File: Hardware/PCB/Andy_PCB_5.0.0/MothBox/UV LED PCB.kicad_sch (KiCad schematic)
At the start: 24 parts, among them J7 DC Power Jack, Q10 BC817, Q11 BC817, Q8 BC817, Q9 BC817, U10 IRF9335TRPBF, U11 IRF9335TRPBF, U8 IRF9335TRPBF, U9 IRF9335TRPBF

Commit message: made better camera
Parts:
- renumbered D29 to D30, D30 to D32, D36 to D33, J7 to J5, Q9 to Q10, Q10 to Q11, Q11 to Q9, R80 to R76, R82 to R78, R76 to R79, R81 to R80, R78 to R81, R79 to R82, U8 to U10, U9 to U12, U10 to U13

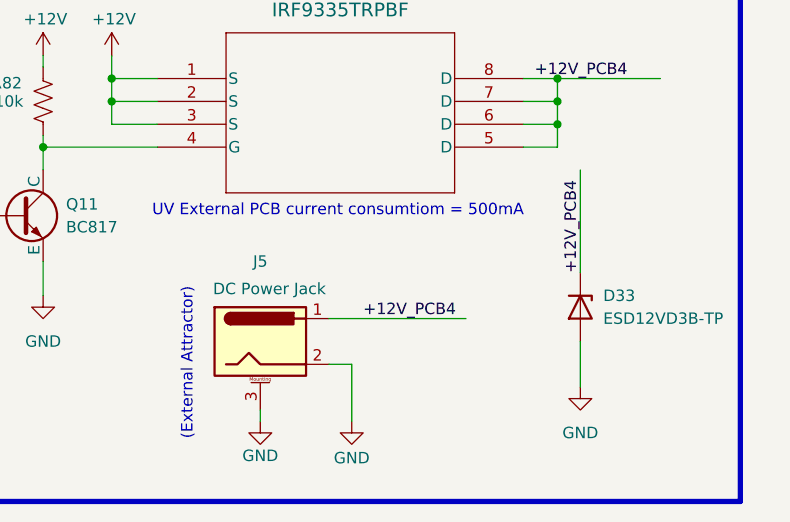
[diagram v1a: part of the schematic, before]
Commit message: added female inverted header
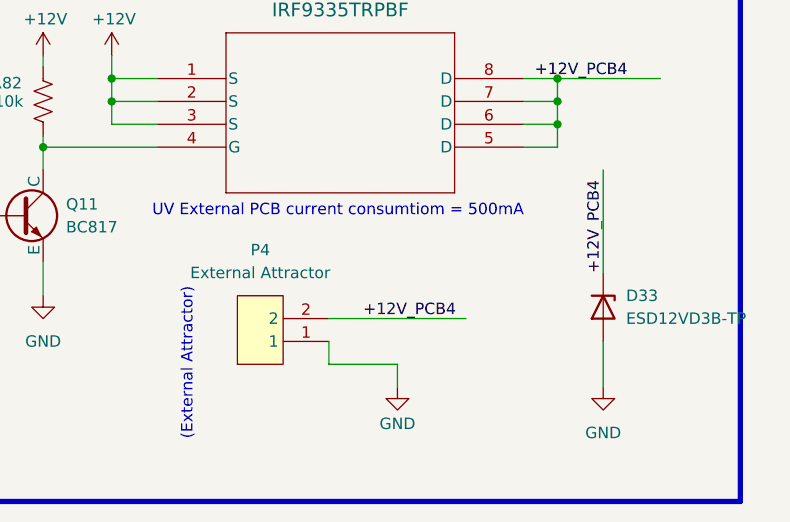
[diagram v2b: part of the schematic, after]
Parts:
- removed J5: DC Power Jack, Connector_BarrelJack:BarrelJack_GCT_DCJ200-10-A_Horizontal, symbol Connector:Barrel_Jack_MountingPin
- added P4: External Attractor, easyeda2kicad:CONN-TH_2P-P5.00_WJ500V-5.08-2P, symbol easyeda2kicad:WJ500V-5.08-2P-14-00A
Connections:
- net +12V_PCB4: now also P4.2
- net GND: now also P4.1
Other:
- moved on the sheet: D33
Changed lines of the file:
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@@
 	(wire
 		(pts
-			(xy 224.79 148.59) (xy 227.33 148.59)
+			(xy 232.41 148.59) (xy 224.79 148.59)
 		)
 		(stroke
@@
 	(wire
 		(pts
-			(xy 252.73 127) (xy 252.73 138.43)
+			(xy 255.27 127) (xy 255.27 138.43)
 		)
 		(stroke
@@
 	(wire
 		(pts
-			(xy 227.33 154.94) (xy 227.33 148.59)
+			(xy 232.41 151.13) (xy 232.41 148.59)
 		)
 		(stroke
@@
 	(wire
 		(pts
+			(xy 224.79 146.05) (xy 224.79 148.59)
+		)
+		(stroke
+			(width 0)
+			(type default)
+		)
+	)
+	(wire
+		(pts
 			(xy 247.65 53.34) (xy 265.43 53.34)
 		)
@@
 	(wire
 		(pts
-			(xy 252.73 146.05) (xy 252.73 151.13)
+			(xy 255.27 146.05) (xy 255.27 151.13)
 		)
 		(stroke
@@
 	(wire
 		(pts
-			(xy 217.17 154.94) (xy 217.17 153.67)
-		)
-		(stroke
-			(width 0)
-			(type default)
-		)
-	)
-	(wire
-		(pts
 			(xy 80.01 55.88) (xy 74.93 55.88)
 		)
@@
 	)
 	(label "+12V_PCB4"
-		(at 252.73 138.43 90)
+		(at 255.27 138.43 90)
 		(effects
 			(font
@@
 	)
 	(symbol
+		(lib_id "easyeda2kicad:WJ500V-5.08-2P-14-00A")
+		(at 219.71 144.78 90)
+		(unit 1)
+		(exclude_from_sim no)
+		(in_bom yes)
+		(on_board yes)
+		(dnp no)
+		(fields_autoplaced yes)
+		(property "Reference" "P4"
+			(at 217.17 135.89 90)
+			(effects
+				(font
+					(size 1.27 1.27)
+				)
+			)
+		)
+		(property "Value" "External Attractor"
+			(at 217.17 138.43 90)
+			(effects
+				(font
+					(size 1.27 1.27)
+				)
+			)
+		)
+		(property "Footprint" "easyeda2kicad:CONN-TH_2P-P5.00_WJ500V-5.08-2P"
+			(at 232.41 144.78 0)
+			(effects
+				(font
+					(size 1.27 1.27)
+				)
+				(hide yes)
+			)
+		)
+		(property "Datasheet" "https://lcsc.com/product-detail/Terminal-Blocks_WJ500V-5-08-2P_C8465.html"
+			(at 234.95 144.78 0)
+			(effects
+				(font
+					(size 1.27 1.27)
+				)
+				(hide yes)
+			)
+		)
+		(property "Description" ""
+			(at 219.71 144.78 0)
+			(effects
+				(font
+					(size 1.27 1.27)
+				)
+				(hide yes)
+			)
+		)
+		(property "LCSC Part" "C8465"
+			(at 237.49 144.78 0)
+			(effects
+				(font
+					(size 1.27 1.27)
+				)
+				(hide yes)
+			)
+		)
+		(pin "2"
+		)
+		(pin "1"
+		)
+		(instances
+			(project "MothBox"
+				(path "/9021e528-fc76-4423-a3f3-30f5652071cc/25f161be-2136-4f06-bcb6-1cc6303e8ec0"
+					(reference "P4")
+					(unit 1)
+				)
+			)
+		)
+	)
+	(symbol
 		(lib_id "power:+12V")
 		(at 67.31 116.84 0)
@@
 	(symbol
 		(lib_id "power:GND")
-		(at 217.17 154.94 0)
-		(unit 1)
-		(exclude_from_sim no)
-		(in_bom yes)
-		(on_board yes)
-		(dnp no)
-		(property "Reference" "#PWR099"
-			(at 217.17 161.29 0)
-			(effects
-				(font
-					(size 1.27 1.27)
-				)
-				(hide yes)
-			)
-		)
-		(property "Value" "GND"
-			(at 217.17 158.75 0)
-			(effects
-				(font
-					(size 1.27 1.27)
-				)
-			)
-		)
-		(property "Footprint" ""
-			(at 217.17 154.94 0)
-			(effects
-				(font
-					(size 1.27 1.27)
-				)
-				(hide yes)
-			)
-		)
-		(property "Datasheet" ""
-			(at 217.17 154.94 0)
-			(effects
-				(font
-					(size 1.27 1.27)
-				)
-				(hide yes)
-			)
-		)
-		(property "Description" "Power symbol creates a global label with name \"GND\" , ground"
-			(at 217.17 154.94 0)
-			(effects
-				(font
-					(size 1.27 1.27)
-				)
-				(hide yes)
-			)
-		)
-		(pin "1"
-		)
-		(instances
-			(project "MothBo"
-				(path "/9021e528-fc76-4423-a3f3-30f5652071cc/25f161be-2136-4f06-bcb6-1cc6303e8ec0"
-					(reference "#PWR099")
-					(unit 1)
-				)
-			)
-		)
-	)
-	(symbol
-		(lib_id "power:GND")
 		(at 129.54 151.13 0)
 		(unit 1)
@@
 	(symbol
 		(lib_id "Diode:ESD5Zxx")
-		(at 252.73 142.24 270)
+		(at 255.27 142.24 270)
 		(unit 1)
 		(exclude_from_sim no)
@@
 		(fields_autoplaced yes)
 		(property "Reference" "D33"
-			(at 255.27 140.9699 90)
+			(at 257.81 140.9699 90)
 			(effects
 				(font
@@
 		)
 		(property "Value" "ESD12VD3B-TP"
-			(at 255.27 143.5099 90)
+			(at 257.81 143.5099 90)
 			(effects
 				(font
@@
 		)
 		(property "Footprint" "Diode_SMD:D_SOD-323"
-			(at 248.285 142.24 0)
+			(at 250.825 142.24 0)
 			(effects
 				(font
@@
 		)
 		(property "Datasheet" "https://www.lcsc.com/datasheet/lcsc_datasheet_2410121813_MCC-Micro-Commercial-Components-ESD12VD3B-TP_C435886.pdf"
-			(at 252.73 142.24 0)
+			(at 255.27 142.24 0)
 			(effects
 				(font
@@
 		)
 		(property "Description" "15.5V 350W 13.5V 12V SOD-323 ESD and Surge Protection (TVS/ESD) ROHS"
-			(at 252.73 142.24 0)
+			(at 255.27 142.24 0)
 			(effects
 				(font
@@
 		)
 		(property "LCSC Part no " "C435886"
-			(at 252.73 142.24 0)
+			(at 255.27 142.24 0)
 			(effects
 				(font
@@
 		)
 		(property "LCSC PN" ""
-			(at 252.73 142.24 0)
+			(at 255.27 142.24 0)
 			(effects
 				(font
@@
 	(symbol
 		(lib_id "power:GND")
-		(at 252.73 151.13 0)
+		(at 255.27 151.13 0)
 		(unit 1)
 		(exclude_from_sim no)
@@
 		(fields_autoplaced yes)
 		(property "Reference" "#PWR0102"
-			(at 252.73 157.48 0)
+			(at 255.27 157.48 0)
 			(effects
 				(font
@@
 		)
 		(property "Value" "GND"
-			(at 252.73 156.21 0)
+			(at 255.27 156.21 0)
 			(effects
 				(font
@@
 		)
 		(property "Footprint" ""
-			(at 252.73 151.13 0)
+			(at 255.27 151.13 0)
 			(effects
 				(font
@@
 		)
 		(property "Datasheet" ""
-			(at 252.73 151.13 0)
+			(at 255.27 151.13 0)
 			(effects
 				(font
@@
 		)
 		(property "Description" "Power symbol creates a global label with name \"GND\" , ground"
-			(at 252.73 151.13 0)
+			(at 255.27 151.13 0)
 			(effects
 				(font
@@
 	(symbol
 		(lib_id "power:GND")
-		(at 227.33 154.94 0)
+		(at 232.41 151.13 0)
 		(unit 1)
 		(exclude_from_sim no)
@@
 		(dnp no)
 		(property "Reference" "#PWR0100"
-			(at 227.33 161.29 0)
+			(at 232.41 157.48 0)
 			(effects
 				(font
@@
 		)
 		(property "Value" "GND"
-			(at 227.33 159.004 0)
+			(at 232.41 155.194 0)
 			(effects
 				(font
@@
 		)
 		(property "Footprint" ""
-			(at 227.33 154.94 0)
+			(at 232.41 151.13 0)
 			(effects
 				(font
@@
 		)
 		(property "Datasheet" ""
-			(at 227.33 154.94 0)
+			(at 232.41 151.13 0)
 			(effects
 				(font
@@
 		)
 		(property "Description" "Power symbol creates a global label with name \"GND\" , ground"
-			(at 227.33 154.94 0)
+			(at 232.41 151.13 0)
 			(effects
 				(font
@@
 					(unit 1)
 				)
-			)
-		)
-	)
-	(symbol
-		(lib_id "Connector:Barrel_Jack_MountingPin")
-		(at 217.17 146.05 0)
-		(unit 1)
-		(exclude_from_sim no)
-		(in_bom yes)
-		(on_board yes)
-		(dnp no)
-		(property "Reference" "J5"
-			(at 217.17 137.16 0)
-			(effects
-				(font
-					(size 1.27 1.27)
-				)
-			)
-		)
-		(property "Value" "DC Power Jack"
-			(at 218.186 140.208 0)
-			(effects
-				(font
-					(size 1.27 1.27)
-				)
-			)
-		)
-		(property "Footprint" "Connector_BarrelJack:BarrelJack_GCT_DCJ200-10-A_Horizontal"
-			(at 218.44 147.066 0)
-			(effects
-				(font
-					(size 1.27 1.27)
-				)
-				(hide yes)
-			)
-		)
-		(property "Datasheet" "~"
-			(at 218.44 147.066 0)
-			(effects
-				(font
-					(size 1.27 1.27)
-				)
-				(hide yes)
-			)
-		)
-		(property "Description" "DC Barrel Jack with a mounting pin"
-			(at 217.17 146.05 0)
-			(effects
-				(font
-					(size 1.27 1.27)
-				)
-				(hide yes)
-			)
-		)
-		(property "LCSC Part no " "C319099"
-			(at 217.17 146.05 0)
-			(effects
-				(font
-					(size 1.27 1.27)
-				)
-				(hide yes)
-			)
-		)
-		(property "Digikey Part No" "486-3381-ND"
-			(at 217.17 146.05 0)
-			(effects
-				(font
-					(size 1.27 1.27)
-				)
-				(hide yes)
-			)
-		)
-		(property "LCSC PN" ""
-			(at 217.17 146.05 0)
-			(effects
-				(font
-					(size 1.27 1.27)
-				)
-			)
-		)
-		(pin "3"
-		)
-		(pin "2"
-		)
-		(pin "1"
-		)
-		(instances
-			(project "MothBo"
-				(path "/9021e528-fc76-4423-a3f3-30f5652071cc/25f161be-2136-4f06-bcb6-1cc6303e8ec0"
-					(reference "J5")
-					(unit 1)
-				)

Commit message: arranged stuff better
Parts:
- P4: footprint easyeda2kicad:CONN-TH_2P-P5.00_WJ500V-5.08-2P -> easyeda2kicad:CONN-TH_DB301V-3.5-2P-GN; symbol easyeda2kicad:WJ500V-5.08-2P-14-00A -> easyeda2kicad:DB301V-3.5-2P-GN; LCSC Part C8465 -> C695629
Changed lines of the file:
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@@
 	)
 	(symbol
-		(lib_id "easyeda2kicad:WJ500V-5.08-2P-14-00A")
-		(at 219.71 144.78 90)
+		(lib_id "easyeda2kicad:DB301V-3.5-2P-GN")
+		(at 219.71 144.78 180)
 		(unit 1)
 		(exclude_from_sim no)
@@
 		(fields_autoplaced yes)
 		(property "Reference" "P4"
-			(at 217.17 135.89 90)
+			(at 219.71 135.89 0)
 			(effects
 				(font
@@
 		)
 		(property "Value" "External Attractor"
-			(at 217.17 138.43 90)
+			(at 219.71 138.43 0)
 			(effects
 				(font
@@
 			)
 		)
-		(property "Footprint" "easyeda2kicad:CONN-TH_2P-P5.00_WJ500V-5.08-2P"
-			(at 232.41 144.78 0)
+		(property "Footprint" "easyeda2kicad:CONN-TH_DB301V-3.5-2P-GN"
+			(at 219.71 135.89 0)
 			(effects
 				(font
@@
 			)
 		)
-		(property "Datasheet" "https://lcsc.com/product-detail/Terminal-Blocks_WJ500V-5-08-2P_C8465.html"
-			(at 234.95 144.78 0)
+		(property "Datasheet" "https://lcsc.com/product-detail/Wire-To-Board-Wire-To-Wire-Connector_DIBO-DB301V-3-5-2P-GN_C695629.html"
+			(at 219.71 133.35 0)
 			(effects
 				(font
@@
 			)
 		)
-		(property "LCSC Part" "C8465"
-			(at 237.49 144.78 0)
+		(property "LCSC Part" "C695629"
+			(at 219.71 130.81 0)
 			(effects
 				(font
